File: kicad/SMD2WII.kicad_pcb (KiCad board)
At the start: 2 copper layers, 31.1 x 54.4 mm, 13 parts, among them J2 DB9_Male, J3 Conn_01x06_Pin, U1 ATmega8A-A

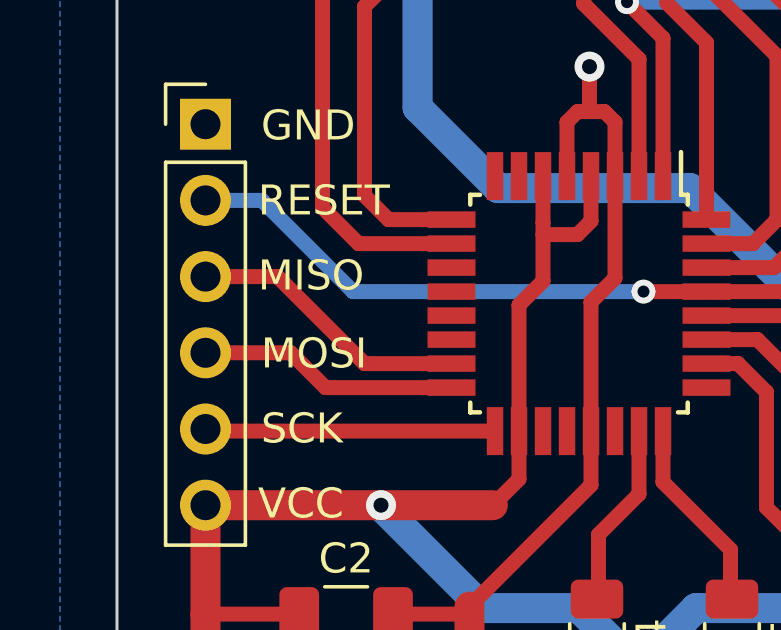
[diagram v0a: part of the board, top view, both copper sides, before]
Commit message: Swap MISO <=> MOSI.
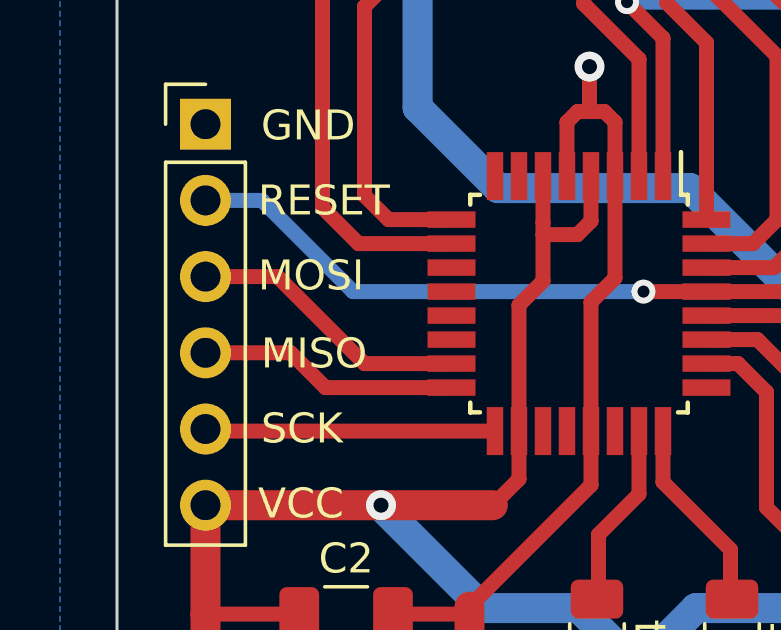
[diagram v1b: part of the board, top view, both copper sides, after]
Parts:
- R2: value 2.2K -> 2.2k
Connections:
- J3 pad 3: /MISO -> /MOSI
- J3 pad 4: /MOSI -> /MISO
- U1 pad 15: /MISO -> /MOSI
- U1 pad 16: /MOSI -> /MISO
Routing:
- net /MOSI: track 8.68 -> 9.40 mm
- net /MISO: track 9.40 -> 8.68 mm
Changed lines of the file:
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@@
     (pcbplotparams
       (layerselection 0x00010fc_ffffffff)
-      (plot_on_all_layers_selection 0x00010fc_80000001)
+      (plot_on_all_layers_selection 0x0000000_00000000)
       (disableapertmacros false)
       (usegerberextensions false)
@@
         (effects (font (size 1 1) (thickness 0.15)))
     )
-    (fp_text value "2.2K" (at 0 1.82 90) (layer "F.Fab")
+    (fp_text value "2.2k" (at 0 1.82 90) (layer "F.Fab")
         (effects (font (size 1 1) (thickness 0.15)))
     )
@@
       (net 27 "unconnected-(U1-PB2-Pad14)") (pinfunction "PB2") (pintype "bidirectional+no_connect"))
     (pad "15" smd rect (at 2 4.25) (size 1.6 0.55) (layers "F.Cu" "F.Paste" "F.Mask")
-      (net 14 "/MISO") (pinfunction "PB3") (pintype "bidirectional"))
+      (net 16 "/MOSI") (pinfunction "PB3") (pintype "bidirectional"))
     (pad "16" smd rect (at 2.8 4.25) (size 1.6 0.55) (layers "F.Cu" "F.Paste" "F.Mask")
-      (net 16 "/MOSI") (pinfunction "PB4") (pintype "bidirectional"))
+      (net 14 "/MISO") (pinfunction "PB4") (pintype "bidirectional"))
     (pad "17" smd rect (at 4.25 2.8 270) (size 1.6 0.55) (layers "F.Cu" "F.Paste" "F.Mask")
       (net 15 "/SCK") (pinfunction "PB5") (pintype "bidirectional"))
@@
       (net 17 "RESET") (pinfunction "Pin_2") (pintype "passive"))
     (pad "3" thru_hole oval (at 0 5.08) (size 1.7 1.7) (drill 1) (layers "*.Cu" "*.Mask")
-      (net 14 "/MISO") (pinfunction "Pin_3") (pintype "passive"))
+      (net 16 "/MOSI") (pinfunction "Pin_3") (pintype "passive"))
     (pad "4" thru_hole oval (at 0 7.62) (size 1.7 1.7) (drill 1) (layers "*.Cu" "*.Mask")
-      (net 16 "/MOSI") (pinfunction "Pin_4") (pintype "passive"))
+      (net 14 "/MISO") (pinfunction "Pin_4") (pintype "passive"))
     (pad "5" thru_hole oval (at 0 10.16) (size 1.7 1.7) (drill 1) (layers "*.Cu" "*.Mask")
       (net 15 "/SCK") (pinfunction "Pin_5") (pintype "passive"))
@@
     (effects (font (size 0.75 0.75) (thickness 0.1)) (justify left bottom mirror))
   )
-  (gr_text "MOSI" (at 102.9 81) (layer "F.SilkS")
+  (gr_text "MISO" (at 102.9 81) (layer "F.SilkS")
     (effects (font (size 1 1) (thickness 0.15)) (justify left bottom))
   )
@@
     (effects (font (size 1 1) (thickness 0.15)) (justify left bottom))
   )
-  (gr_text "MISO" (at 102.8 78.4) (layer "F.SilkS")
+  (gr_text "MOSI" (at 102.8 78.4) (layer "F.SilkS")
     (effects (font (size 1 1) (thickness 0.15)) (justify left bottom))
   )
@@
   (segment (start 105.8 63) (end 107.109669 61.690331) (width 0.5) (layer "F.Cu") (net 13))
   (segment (start 104.95 66.55) (end 105.8 65.7) (width 0.5) (layer "F.Cu") (net 13))
-  (segment (start 109.25 80.75) (end 106.35 80.75) (width 0.5) (layer "F.Cu") (net 14))
-  (segment (start 106.35 80.75) (end 103.45 77.85) (width 0.5) (layer "F.Cu") (net 14))
-  (segment (start 103.45 77.85) (end 101.05 77.85) (width 0.5) (layer "F.Cu") (net 14))
+  (segment (start 103.89 80.39) (end 101.05 80.39) (width 0.5) (layer "F.Cu") (net 14))
+  (segment (start 109.25 81.55) (end 105.05 81.55) (width 0.5) (layer "F.Cu") (net 14))
+  (segment (start 105.05 81.55) (end 103.89 80.39) (width 0.5) (layer "F.Cu") (net 14))
   (segment (start 110.7 83) (end 101.12 83) (width 0.5) (layer "F.Cu") (net 15))
   (segment (start 101.12 83) (end 101.05 82.93) (width 0.35) (layer "F.Cu") (net 15))
-  (segment (start 103.89 80.39) (end 101.05 80.39) (width 0.5) (layer "F.Cu") (net 16))
-  (segment (start 109.25 81.55) (end 105.05 81.55) (width 0.5) (layer "F.Cu") (net 16))
-  (segment (start 105.05 81.55) (end 103.89 80.39) (width 0.5) (layer "F.Cu") (net 16))
+  (segment (start 109.25 80.75) (end 106.35 80.75) (width 0.5) (layer "F.Cu") (net 16))
+  (segment (start 106.35 80.75) (end 103.45 77.85) (width 0.5) (layer "F.Cu") (net 16))
+  (segment (start 103.45 77.85) (end 101.05 77.85) (width 0.5) (layer "F.Cu") (net 16))
   (segment (start 122.6 78.35) (end 123.6 77.35) (width 0.5) (layer "F.Cu") (net 17))
   (segment (start 117.75 78.35) (end 122.6 78.35) (width 0.5) (layer "F.Cu") (net 17))

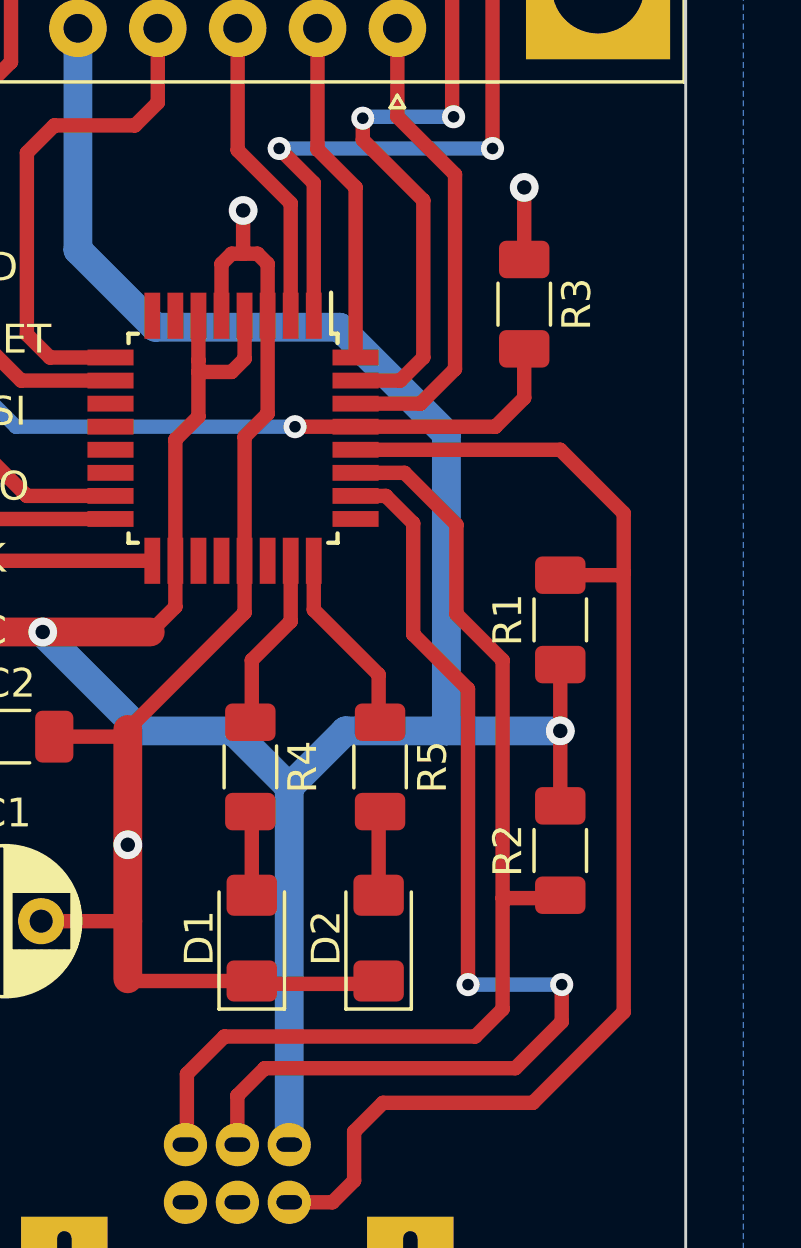
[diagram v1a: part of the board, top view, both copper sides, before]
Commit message: Connect RESET to VCC instead of GND.
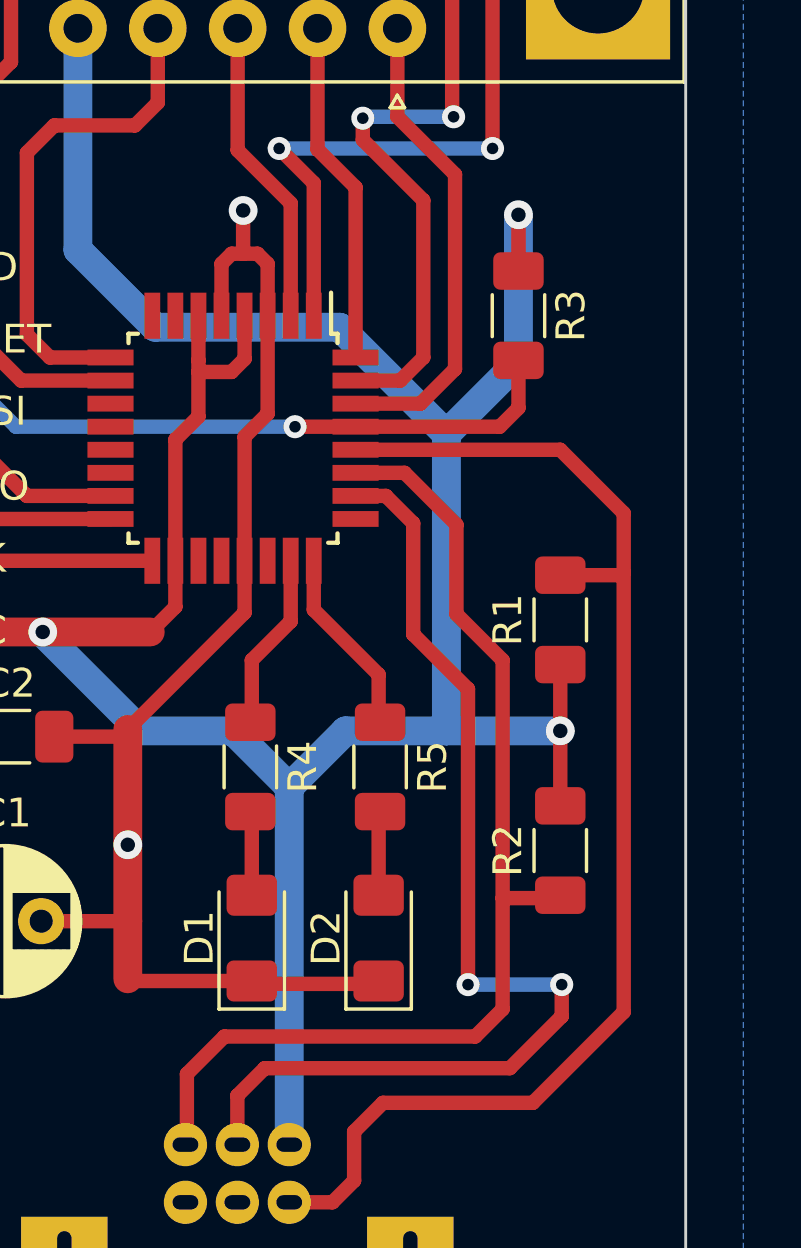
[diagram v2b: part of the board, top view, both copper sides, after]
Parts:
- moved R3 0.45 mm to (123.4, 74.5)
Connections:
- R3 pad 1: GND -> VCC
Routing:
- net VCC: track 112.2 -> 122.8 mm, vias 2 -> 3
- net GND: track 48.7 -> 46.2 mm, vias 3 -> 2
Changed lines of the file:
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@@
   )
   (footprint "Resistor_SMD:R_1206_3216Metric_Pad1.30x1.75mm_HandSolder" (layer "F.Cu")
-    (at 123.6 74.1 -90)
+    (at 123.4 74.5 -90)
     (descr "Resistor SMD 1206 (3216 Metric), square (rectangular) end terminal, IPC_7351 nominal with elongated pad for handsoldering. (Body size source: IPC-SM-782 page 72, https://www.pcb-3d.com/wordpress/wp-content/uploads/ipc-sm-782a_amendment_1_and_2.pdf), generated with kicad-footprint-generator")
     (tags "resistor handsolder")
@@
       (stroke (width 0.1) (type solid)) (layer "F.Fab"))
     (pad "1" smd roundrect (at -1.55 0 270) (size 1.3 1.75) (layers "F.Cu" "F.Paste" "F.Mask") (roundrect_rratio 0.1923076923)
-      (net 2 "GND") (pintype "passive"))
+      (net 1 "VCC") (pintype "passive"))
     (pad "2" smd roundrect (at 1.55 0 270) (size 1.3 1.75) (layers "F.Cu" "F.Paste" "F.Mask") (roundrect_rratio 0.1923076923)
       (net 17 "RESET") (pintype "passive"))
@@
   (segment (start 110.63 85.47) (end 111.5 84.6) (width 0.5) (layer "F.Cu") (net 1))
   (segment (start 124.85 88.9) (end 124.85 91.5) (width 0.5) (layer "F.Cu") (net 1))
+  (segment (start 123.4 72.95) (end 123.4 71) (width 0.5) (layer "F.Cu") (net 1))
   (via (at 124.85 88.9) (size 1) (drill 0.5) (layers "F.Cu" "B.Cu") (net 1))
+  (via (at 123.4 71) (size 1) (drill 0.5) (layers "F.Cu" "B.Cu") (net 1))
   (via (at 106.9 85.47) (size 1) (drill 0.5) (layers "F.Cu" "B.Cu") (net 1))
+  (segment (start 123.4 76.1) (end 123.4 71) (width 1) (layer "B.Cu") (net 1))
   (segment (start 117.4 88.9) (end 120.9 88.9) (width 1) (layer "B.Cu") (net 1))
+  (segment (start 120.9 78.6) (end 123.4 76.1) (width 1) (layer "B.Cu") (net 1))
   (segment (start 106.9 85.5) (end 110.3 88.9) (width 1) (layer "B.Cu") (net 1))
   (segment (start 117.2 74.9) (end 110.8 74.9) (width 1) (layer "B.Cu") (net 1))
@@
   (segment (start 113.5 88.9) (end 115.45 90.85) (width 1) (layer "B.Cu") (net 1))
   (segment (start 110.3 88.9) (end 113.5 88.9) (width 1) (layer "B.Cu") (net 1))
-  (segment (start 123.6 72.55) (end 123.6 70.05) (width 0.5) (layer "F.Cu") (net 2))
   (segment (start 113.9 83) (end 113.9 84.8) (width 0.5) (layer "F.Cu") (net 2))
   (segment (start 114.7 72.7) (end 114.7 74.5) (width 0.5) (layer "F.Cu") (net 2))
@@
   (segment (start 113.9 84.8) (end 109.85 88.85) (width 0.5) (layer "F.Cu") (net 2))
   (via (at 113.85 70.85) (size 1) (drill 0.5) (layers "F.Cu" "B.Cu") (net 2))
-  (via (at 123.6 70.05) (size 1) (drill 0.5) (layers "F.Cu" "B.Cu") (net 2))
   (via (at 109.85 92.85) (size 1) (drill 0.5) (layers "F.Cu" "B.Cu") (net 2))
   (segment (start 121.65 87.45) (end 119.75 85.55) (width 0.5) (layer "F.Cu") (net 3))
   (segment (start 119.75 85.55) (end 119.75 81.7) (width 0.5) (layer "F.Cu") (net 3))
+  (segment (start 124.9 98.8) (end 123.1 100.6) (width 0.5) (layer "F.Cu") (net 3))
+  (segment (start 113.65 101.55) (end 113.65 103.25) (width 0.5) (layer "F.Cu") (net 3))
   (segment (start 113.55 103.25) (end 113.6 103.2) (width 0.5) (layer "F.Cu") (net 3))
-  (segment (start 124.9 97.7) (end 124.9 98.989949) (width 0.5) (layer "F.Cu") (net 3))
-  (segment (start 123.289949 100.6) (end 114.6 100.6) (width 0.5) (layer "F.Cu") (net 3))
-  (segment (start 124.9 98.989949) (end 123.289949 100.6) (width 0.5) (layer "F.Cu") (net 3))
+  (segment (start 124.9 97.7) (end 124.9 98.8) (width 0.5) (layer "F.Cu") (net 3))
+  (segment (start 114.6 100.6) (end 113.65 101.55) (width 0.5) (layer "F.Cu") (net 3))
   (segment (start 118.8 80.75) (end 117.75 80.75) (width 0.5) (layer "F.Cu") (net 3))
   (segment (start 119.75 81.7) (end 118.8 80.75) (width 0.5) (layer "F.Cu") (net 3))
   (segment (start 121.65 97.7) (end 121.65 87.45) (width 0.5) (layer "F.Cu") (net 3))
-  (segment (start 114.6 100.6) (end 113.65 101.55) (width 0.5) (layer "F.Cu") (net 3))
-  (segment (start 113.65 101.55) (end 113.65 103.25) (width 0.5) (layer "F.Cu") (net 3))
+  (segment (start 123.1 100.6) (end 114.6 100.6) (width 0.5) (layer "F.Cu") (net 3))
   (via (at 124.9 97.7) (size 0.8) (drill 0.4) (layers "F.Cu" "B.Cu") (net 3))
   (via (at 121.65 97.7) (size 0.8) (drill 0.4) (layers "F.Cu" "B.Cu") (net 3))
@@
   (segment (start 106.35 80.75) (end 103.45 77.85) (width 0.5) (layer "F.Cu") (net 16))
   (segment (start 103.45 77.85) (end 101.05 77.85) (width 0.5) (layer "F.Cu") (net 16))
-  (segment (start 122.6 78.35) (end 123.6 77.35) (width 0.5) (layer "F.Cu") (net 17))
-  (segment (start 117.75 78.35) (end 122.6 78.35) (width 0.5) (layer "F.Cu") (net 17))
-  (segment (start 123.6 77.35) (end 123.6 75.65) (width 0.5) (layer "F.Cu") (net 17))
+  (segment (start 123.4 77.7) (end 123.4 76.05) (width 0.5) (layer "F.Cu") (net 17))
+  (segment (start 117.75 78.35) (end 122.75 78.35) (width 0.5) (layer "F.Cu") (net 17))
+  (segment (start 122.75 78.35) (end 123.4 77.7) (width 0.5) (layer "F.Cu") (net 17))
   (segment (start 115.65 78.35) (end 117.75 78.35) (width 0.5) (layer "F.Cu") (net 17))
   (via (at 115.65 78.35) (size 0.8) (drill 0.4) (layers "F.Cu" "B.Cu") (net 17))

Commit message: Compact PCB.
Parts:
- moved J1 9.85 mm to (113.7, 110.4)
- moved D1 9.62 mm to (111.3, 86.9), turned to -90 degrees
- moved D2 9.33 mm to (116.9, 86.9), turned to -90 degrees
- moved R2 6.15 mm to (124.8, 86.9)
- moved R1 5.85 mm to (124.8, 79.2)
- moved C1 4.41 mm to (104.1, 91.1)
- moved C2 3.83 mm to (105.3, 85.3)
- moved R5 3.43 mm to (119.7, 86.9)
- moved J3 3.30 mm to (101.0, 69.5)
- moved U1 3.30 mm to (113.5, 75.5)
- moved R4 3.25 mm to (114.1, 86.9)
- moved R3 2.30 mm to (124.9, 72.8)
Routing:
- net /DTC: track 37.6 -> 25.8 mm
- net VCC: track 122.8 -> 111.7 mm, vias 3 -> 2
- net /SDA: track 38.1 -> 31.8 mm
- net GND: track 46.2 -> 40.4 mm, vias 2 -> 3
- net /SCL: track 45.1 -> 39.5 mm
- net /SMD_SELECT: track 31.5 -> 26.5 mm
- net /SMD_D2: track 10.7 -> 7.43 mm
- net /SMD_D1: track 12.0 -> 8.67 mm
- net /SMD_D3: track 17.4 -> 14.1 mm
- net /SMD_D0: track 16.6 -> 13.3 mm
- net /SMD_D5: track 21.9 -> 18.6 mm
- net /SMD_D4: track 23.5 -> 20.2 mm
- net Net-(U1-PC1): track 6.38 -> 7.47 mm
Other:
- board size 31.1 x 54.4 mm -> 31.1 x 44.5 mm

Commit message: Re-use C1 pin for front side GND.
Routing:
- net GND: track 40.4 -> 43.0 mm, vias 3 -> 2
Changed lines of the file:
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@@
   (segment (start 113.9 79.7) (end 113.9 81.2) (width 0.5) (layer "F.Cu") (net 2))
   (segment (start 114.7 69.4) (end 114.7 71.2) (width 0.5) (layer "F.Cu") (net 2))
+  (segment (start 109.2 93.81066) (end 109.2 91.1) (width 1) (layer "F.Cu") (net 2))
   (segment (start 113.45 69.05) (end 113.1 69.4) (width 0.5) (layer "F.Cu") (net 2))
   (segment (start 106.8625 85.3) (end 109.2 85.3) (width 0.5) (layer "F.Cu") (net 2))
-  (segment (start 109.2 93.81066) (end 109.2 87.2) (width 1) (layer "F.Cu") (net 2))
+  (segment (start 109.2 91.1) (end 109.2 87.2) (width 1) (layer "F.Cu") (net 2))
   (segment (start 111.3 85.4125) (end 109.3125 85.4125) (width 0.5) (layer "F.Cu") (net 2))
   (segment (start 109.2 84.3) (end 109.7 83.8) (width 1) (layer "F.Cu") (net 2))
   (segment (start 109.2 87.2) (end 109.2 85.3) (width 1) (layer "F.Cu") (net 2))
+  (segment (start 106.594888 91.1) (end 109.2 91.1) (width 0.5) (layer "F.Cu") (net 2))
   (segment (start 109.2 85.3) (end 109.2 84.3) (width 1) (layer "F.Cu") (net 2))
   (segment (start 110.78934 95.4) (end 109.2 93.81066) (width 1) (layer "F.Cu") (net 2))
@@
   (segment (start 113.9 81.2) (end 111.5 83.6) (width 0.5) (layer "F.Cu") (net 2))
   (segment (start 113.1 69.4) (end 113.1 71.2) (width 0.5) (layer "F.Cu") (net 2))
-  (via (at 109.2 87.2) (size 0.8) (drill 0.4) (layers "F.Cu" "B.Cu") (net 2))
   (via (at 113.85 69.05) (size 1) (drill 0.5) (layers "F.Cu" "B.Cu") (net 2))
   (via (at 116.9 83.2) (size 0.8) (drill 0.4) (layers "F.Cu" "B.Cu") (net 2))
